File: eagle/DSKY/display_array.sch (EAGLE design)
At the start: 65 parts, among them IC1 PCF8574T, IC10 PCF8574AT, IC2 PCF8574T, IC3 PCF8574T, IC4 PCF8574T, IC5 PCF8574T, IC6 PCF8574T, IC7 PCF8574T, IC8 PCF8574T, IC9 PCF8574AT

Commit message: brightness control
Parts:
- removed RN17: (no value), be_rcl:R_EU_ARRAY_1C_8_T_SIL9
- added C1201, C1202, C1203, C1204, C1301, C1302, C1303, C1304: 10u, be_rcl:C_POL_EU_T_RAD5_GRID_2.54
- added C1205, C1206, C1305, C1306: 100n, be_rcl:C_EU_S_0805
- added H1101, H1102, H1103, H1104: HOLE_4.1_PAD, be_holes:HOLE_4.1_PAD
- added IC1201, IC1202, IC1301, IC1302: (no value), be_logic:7400N
- added RN1001, RN1002: 100, be_rcl:R_EU_ARRAY_4
- added RN1201, RN1202, RN1301, RN1302: 220, be_rcl:R_EU_ARRAY_4
- added RN1203, RN1303: 4k7, be_rcl:R_EU_ARRAY_4
- renumbered C1 to C101, C10 to C1001, C2 to C201, C3 to C301, C4 to C401, C5 to C501, C6 to C601, C7 to C701, C8 to C801, C9 to C901, DIS1 to DIS101, DIS2 to DIS201, DIS3 to DIS301, DIS4 to DIS401, DIS5 to DIS501, DIS6 to DIS601, DIS7 to DIS701, DIS8 to DIS801, IC1 to IC101, IC10 to IC1001, IC2 to IC201, IC3 to IC301, IC4 to IC401, IC5 to IC501, IC6 to IC601, IC7 to IC701, IC8 to IC801, IC9 to IC901, LED1 to LED902, LED10 to LED903, LED12 to LED910, LED2 to LED909, LED3 to LED908, LED4 to LED911, LED5 to LED901, LED6 to LED906, LED7 to LED907, LED8 to LED905, LED9 to LED904, R1 to R909, R2 to R908, R3 to R907, R4 to R906, R5 to R905, R6 to R904, R7 to R903, R8 to R902, R9 to R901, RN1 to RN101, RN10 to RN502, RN11 to RN601, RN12 to RN602, RN13 to RN701, RN14 to RN702, RN15 to RN801, RN16 to RN802, RN2 to RN102, RN3 to RN201, RN4 to RN202, RN5 to RN301, RN6 to RN302, RN7 to RN401, RN8 to RN402, RN9 to RN501
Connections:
- new net DEBOUNCER_10: C1201.+, RN1201A.2, RN1201B.1
- new net DEBOUNCER_11: IC1201A.I0, IC1201A.I1, RN1201B.2, RN1203B.1
- new net DEBOUNCER_12: IC1201A.O, IC1201B.I0, IC1201B.I1
- new net DEBOUNCER_1_OUT#: IC1201B.O, RN1001A.2, RN1203B.2
- new net DEBOUNCER_20: C1202.+, RN1201C.2, RN1201D.1
- new net DEBOUNCER_21: IC1201D.I0, IC1201D.I1, RN1201D.2, RN1203A.1
- new net DEBOUNCER_22: IC1201C.I0, IC1201C.I1, IC1201D.O
- new net DEBOUNCER_2_OUT#: IC1201C.O, RN1001B.2, RN1203A.2
- new net DEBOUNCER_30: C1203.+, RN1202A.2, RN1202B.1
- new net DEBOUNCER_31: IC1202A.I0, IC1202A.I1, RN1202B.2, RN1203C.1
- new net DEBOUNCER_32: IC1202A.O, IC1202B.I0, IC1202B.I1
- new net DEBOUNCER_3_OUT#: IC1202B.O, RN1001C.2, RN1203C.2
- new net DEBOUNCER_40: C1204.+, RN1202C.2, RN1202D.1
- new net DEBOUNCER_41: IC1202D.I0, IC1202D.I1, RN1202D.2, RN1203D.1
- new net DEBOUNCER_42: IC1202C.I0, IC1202C.I1, IC1202D.O
- new net DEBOUNCER_4_OUT#: IC1202C.O, RN1001D.2, RN1203D.2
- new net DEBOUNCER_50: C1301.+, RN1301A.2, RN1301B.1
- new net DEBOUNCER_51: IC1301A.I0, IC1301A.I1, RN1301B.2, RN1303B.1
- new net DEBOUNCER_52: IC1301A.O, IC1301B.I0, IC1301B.I1
- new net DEBOUNCER_5_OUT#: IC1301B.O, RN1002A.2, RN1303B.2
- new net DEBOUNCER_60: C1302.+, RN1301C.2, RN1301D.1
- new net DEBOUNCER_61: IC1301D.I0, IC1301D.I1, RN1301D.2, RN1303A.1
- new net DEBOUNCER_62: IC1301C.I0, IC1301C.I1, IC1301D.O
- new net DEBOUNCER_6_OUT#: IC1301C.O, RN1002B.2, RN1303A.2
- new net DEBOUNCER_70: C1303.+, RN1302A.2, RN1302B.1
- new net DEBOUNCER_71: IC1302A.I0, IC1302A.I1, RN1302B.2, RN1303C.1
- new net DEBOUNCER_72: IC1302A.O, IC1302B.I0, IC1302B.I1
- new net DEBOUNCER_7_OUT#: IC1302B.O, RN1002C.2, RN1303C.2
- new net DEBOUNCER_80: C1304.+, RN1302C.2, RN1302D.1
- new net DEBOUNCER_81: IC1302D.I0, IC1302D.I1, RN1302D.2, RN1303D.1
- new net DEBOUNCER_82: IC1302C.I0, IC1302C.I1, IC1302D.O
- new net DEBOUNCER_8_OUT#: IC1302C.O, RN1002D.2, RN1303D.2
- new net IN_1#: RN1201A.1
- new net IN_2#: RN1201C.1
- new net IN_3#: RN1202A.1
- new net IN_4#: RN1202C.1
- new net IN_5#: RN1301A.1
- new net IN_6#: RN1301C.1
- new net IN_7#: RN1302A.1
- new net IN_8#: RN1302C.1
- net DRV_ANODE: now also LED903.A, LED904.A, LED905.A, LED906.A, LED907.A, LED908.A, LED909.A, LED910.A, LED911.A
- net GND: now also C1201.-, C1202.-, C1203.-, C1204.-, C1205.2, C1206.2, C1301.-, C1302.-, C1303.-, C1304.-, C1305.2, C1306.2, IC1201P.GND, IC1202P.GND, IC1301P.GND, IC1302P.GND
- net KEYPAD_1_K_1: now also RN1001A.1; no longer RN17.2
- net KEYPAD_1_K_2: now also RN1001B.1; no longer RN17.3
- net KEYPAD_1_K_3: now also RN1001C.1; no longer RN17.4
- net KEYPAD_1_K_4: now also RN1001D.1; no longer RN17.5
- net KEYPAD_1_K_5: now also RN1002A.1; no longer RN17.6
- net KEYPAD_1_K_6: now also RN1002B.1; no longer RN17.7
- net KEYPAD_1_K_7: now also RN1002C.1; no longer RN17.8
- net KEYPAD_1_K_8: now also RN1002D.1; no longer RN17.9
- net P5V: now also C1205.1, C1206.1, C1305.1, C1306.1, IC1201P.VCC, IC1202P.VCC, IC1301P.VCC, IC1302P.VCC; no longer LED903.A, LED904.A, LED905.A, LED906.A, LED907.A, LED908.A, LED909.A, LED910.A, LED911.A, RN17.1

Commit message: added connectors
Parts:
- added C1, C2: 100u, be_rcl:C_POL_EU_T_RAD7_GRID_2.54
- added LED1: green, be_opt:LED_S_0805
- added R1: 220, be_rcl:R_EU_S_0805
- added RN1, RN2: (no value), be_rcl:R_EU_ARRAY_1C_8_T_SIL9
- added S1, S2, S3, S4, S5, S6, S7, S8: (no value), be_switch:PUSH_BUTTON_T_6X6MM
- added X1, X3: MALE_2X13-T-VERTICAL_2.54MM, be_con_jump:MALE_2X13-T-VERTICAL_2.54MM
- added X2: CLAMP_1X4-T-5MM, be_con_jump:CLAMP_1X4-T-5MM
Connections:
- new net CTRL_ACK#: RN2.3, X1.19
- new net CTRL_B2: RN1.4, X1.7
- new net CTRL_B3: RN1.5, X1.9
- new net CTRL_B4: RN1.6, X1.11
- new net CTRL_B5: RN1.7, X1.13
- new net CTRL_B6: RN1.8, X1.15
- new net CTRL_B7: RN1.9, X1.17
- new net CTRL_BUSY: RN2.4, X1.21
- new net CTRL_STROBE#: RN2.2, X1.1
- new net P5V_LED: LED1.C, R1.2
- net CTRL_SCL: now also RN1.2, X1.3
- net CTRL_SDA: now also RN1.3, X1.5
- net GND: now also C1.-, C2.-, R1.1, S1.A1, S2.A1, S3.A1, S4.A1, S5.A1, S6.A1, S7.A1, S8.A1, X1.10, X1.12, X1.14, X1.16, X1.18, X1.2, X1.20, X1.22, X1.24, X1.26, X1.4, X1.6, X1.8, X2.3, X2.4, X3.10, X3.12, X3.14, X3.16, X3.18, X3.2, X3.20, X3.22, X3.24, X3.26, X3.4, X3.6, X3.8
- net IN_1#: now also S1.B1, X3.3
- net IN_2#: now also S2.B1, X3.5
- net IN_3#: now also S3.B1, X3.7
- net IN_4#: now also S4.B1, X3.9
- net IN_5#: now also S5.B1, X3.11
- net IN_6#: now also S6.B1, X3.13
- net IN_7#: now also S7.B1, X3.15
- net IN_8#: now also S8.B1, X3.17
- net P5V: now also C1.+, C2.+, LED1.A, RN1.1, RN2.1, X2.1, X2.2

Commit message: reverse voltage protection
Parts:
- added C102: 47n, be_rcl:C_EU_S_0805
- added C103: 10n, be_rcl:C_EU_S_0805
- added C3: 100n, be_rcl:C_EU_S_0805
- added D1: (no value), be_diode:SINGLE_T_DO204-2_GRID_14MM
- added D101: BAT48, be_diode:SINGLE_T_DO204_GRID_10MM
- added IC1: NE555V, be_timer:555P
- added R101: 10k, be_rcl:R_EU_S_0805
- added R102: 470k, be_rcl:R_EU_S_0805
- added R103: 1k, be_rcl:R_EU_S_0805
- added T101, T102: NX2301P, be_transistor:P-MOSFET
- added TP101, TP102: (no value), be_con_jump:TEST_POINT_T_LARGE
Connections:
- removed net DRV_ANODE: DIS101.COM1, DIS201.COM1, DIS301.COM1, DIS401.COM1, DIS501.COM1, DIS601.COM1, DIS701.COM1, DIS801.COM1, LED903.A, LED904.A, LED905.A, LED906.A, LED907.A, LED908.A, LED909.A, LED910.A, LED911.A
- new net DRV_ANODE_1: DIS101.COM1, DIS201.COM1, DIS301.COM1, DIS401.COM1, LED903.A, LED904.A, LED905.A, LED906.A, LED907.A, LED908.A, LED909.A, LED910.A, LED911.A, T101.D
- new net DRV_ANODE_2: DIS501.COM1, DIS601.COM1, DIS701.COM1, DIS801.COM1, T102.D
- new net TIM_1: C103.1, IC1.OC, IC1.RST#
- new net TIM_2: C102.1, D101.C, IC1.TRG, IC1.TRSHLD, R101.1
- new net TIM_3: D101.A, IC1.DSCHRG, R101.2, R102.1, TP102.MP
- new net TIM_OUT: IC1.OUT, R103.1, T101.G, T102.G
- net GND: now also C102.2, C103.2, C3.2, D1.A, IC1.GND
- net P5V: now also C3.1, D1.C, IC1.VCC, R102.2, R103.2, T101.S, T102.S, TP101.MP
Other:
- note added: "LDC terminals"

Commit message: prepared routing of P5V and GND
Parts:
- removed D1: (no value), be_diode:SINGLE_T_DO204-2_GRID_14MM
- removed LED1: green, be_opt:LED_S_0805
- removed R1: 220, be_rcl:R_EU_S_0805
- added D1401: 1N5400, be_diode:SINGLE_T_DO201_GRID_18MM
- added FD1101, FD1102: FIDUCIAL_CROSSHAIR, be_marks:FIDUCIAL_CROSSHAIR
- added LED1401: green, be_opt:LED_S_0805
- added R1401: 220, be_rcl:R_EU_S_0805
- IC1201, IC1202, IC1301, IC1302: value (none) -> SN7400N; PART_CODE_BEL (none) -> IC_PAC_T_NDIP14_VAL_SN7400N
- R901, R902: value (none) -> 1k5; PART_CODE_BEL (none) -> R_PAC_S_0805_VAL_1k5
- R903, R904: value (none) -> 750; PART_CODE_BEL (none) -> R_PAC_S_0805_VAL_750
- R905, R906: value (none) -> 2k2; PART_CODE_BEL (none) -> R_PAC_S_0805_VAL_2k2
- R907: value (none) -> 3k3; PART_CODE_BEL (none) -> R_PAC_S_0805_VAL_3k3
- R908, R909: value (none) -> 2k5; PART_CODE_BEL (none) -> R_PAC_S_0805_VAL_2k5
- RN1401, RN1402: value (none) -> 10k; BOM (none) -> NO
- S1501: value (none) -> set; FUNCTION (none) -> SET1
- S1502: value (none) -> set; FUNCTION (none) -> SET2
- S1503: value (none) -> set; FUNCTION (none) -> SET3
- S1504: value (none) -> set; FUNCTION (none) -> SET4
- S1505: value (none) -> set; FUNCTION (none) -> SET5
- S1506: value (none) -> set; FUNCTION (none) -> SET6
- S1507: value (none) -> set; FUNCTION (none) -> SET7
- S1508: value (none) -> set; FUNCTION (none) -> SET8
- TP1601, TP1602: value (none) -> TEST_POINT_T_LARGE
- X1501: FUNCTION KEYPAD -> KEYPAD EXT,
- renumbered C1 to C1401, C102 to C1602, C103 to C1603, C2 to C1402, C3 to C1601, D101 to D1601, IC1 to IC1601, R101 to R1601, R102 to R1602, R103 to R1603, RN1 to RN1401, RN2 to RN1402, S1 to S1501, S2 to S1502, S3 to S1503, S4 to S1504, S5 to S1505, S6 to S1506, S7 to S1507, S8 to S1508, T101 to T1601, T102 to T1602, TP101 to TP1601, TP102 to TP1602, X1 to X1402, X2 to X1401, X3 to X1501
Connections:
- net DRV_ANODE_2: now also LED1401.A
- net GND: now also D1401.A, H1101.MOUNT, H1102.MOUNT, H1103.MOUNT, H1104.MOUNT, R1401.1; no longer D1.A, R1.1
- net P5V: now also D1401.C; no longer D1.C, LED1.A
- net P5V_LED: now also LED1401.C, R1401.2; no longer LED1.C, R1.2

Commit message: silk screen for keys fixed
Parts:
- added LED1, LED2: red, be_opt:LED_S_0805
- added R1: 1k5, be_rcl:R_EU_S_0805
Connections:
- net N$1 renamed DRV_9_LED_R1BB
- net N$2 renamed DRV_9_LED_R1AA
- new net DRV_9_LED_R1C: LED1.C, R1.2
- new net DRV_9_LED_R1CC: LED1.A, LED2.C
- net DRV_9_LED_1: now also R1.1
- net DRV_ANODE_1: now also LED2.A
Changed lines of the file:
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@@
 <part name="GND61" library="be_supply" deviceset="GND" device=""/>
 <part name="GND62" library="be_supply" deviceset="GND" device=""/>
+<part name="R1" library="be_rcl" deviceset="R_EU" device="_S_0805" value="1k5">
+<attribute name="PART_CODE_BEL" value="R_PAC_S_0805_VAL_1k5"/>
+</part>
+<part name="LED1" library="be_opt" deviceset="LED" device="_S_0805" value="red">
+<attribute name="PART_CODE_BEL" value="LED_PAC_S_0805_VAL_red"/>
+</part>
+<part name="LED2" library="be_opt" deviceset="LED" device="_S_0805" value="red">
+<attribute name="PART_CODE_BEL" value="LED_PAC_S_0805_VAL_red"/>
+</part>
 </parts>
 <sheets>
@@
 <attribute name="VALUE" x="170.815" y="102.235" size="1.27" layer="96" font="fixed"/>
 </instance>
+<instance part="R1" gate="G$1" x="134.62" y="142.24"/>
+<instance part="LED1" gate="G$1" x="170.18" y="142.24" smashed="yes" rot="R270">
+<attribute name="NAME" x="170.815" y="143.51" size="1.27" layer="95" font="fixed"/>
+<attribute name="VALUE" x="170.815" y="140.335" size="1.27" layer="96" font="fixed"/>
+</instance>
+<instance part="LED2" gate="G$1" x="182.88" y="142.24" smashed="yes" rot="R270">
+<attribute name="NAME" x="183.515" y="143.51" size="1.27" layer="95" font="fixed"/>
+<attribute name="VALUE" x="183.515" y="140.335" size="1.27" layer="96" font="fixed"/>
+</instance>
 </instances>
 <busses>
@@
 <wire x1="127" y1="134.62" x2="127" y2="127" width="0.1524" layer="91"/>
 <junction x="127" y="127"/>
+<pinref part="R1" gate="G$1" pin="1"/>
+<wire x1="129.54" y1="142.24" x2="127" y2="142.24" width="0.1524" layer="91"/>
+<wire x1="127" y1="142.24" x2="127" y2="134.62" width="0.1524" layer="91"/>
+<junction x="127" y="134.62"/>
 </segment>
 </net>
@@
 </segment>
 </net>
-<net name="N$1" class="0">
+<net name="DRV_9_LED_R1BB" class="0">
 <segment>
 <pinref part="LED911" gate="G$1" pin="C"/>
@@
 </segment>
 </net>
-<net name="N$2" class="0">
+<net name="DRV_9_LED_R1AA" class="0">
 <segment>
 <pinref part="LED910" gate="G$1" pin="C"/>
@@
 <pinref part="LED909" gate="G$1" pin="A"/>
 <label x="208.28" y="127" size="1.27" layer="95" font="fixed" xref="yes"/>
-</segment>
-</net>
+<pinref part="LED2" gate="G$1" pin="A"/>
+<wire x1="185.42" y1="142.24" x2="193.04" y2="142.24" width="0.1524" layer="91"/>
+<wire x1="193.04" y1="142.24" x2="193.04" y2="134.62" width="0.1524" layer="91"/>
+<junction x="193.04" y="134.62"/>
+</segment>
+</net>
+<net name="DRV_9_LED_R1C" class="0">
+<segment>
+<pinref part="R1" gate="G$1" pin="2"/>
+<pinref part="LED1" gate="G$1" pin="C"/>
+<wire x1="139.7" y1="142.24" x2="165.1" y2="142.24" width="0.1524" layer="91"/>
+<label x="142.875" y="142.875" size="1.27" layer="95" font="fixed"/>
+</segment>
+</net>
+<net name="DRV_9_LED_R1CC" class="0">
+<segment>
+<pinref part="LED1" gate="G$1" pin="A"/>
+<pinref part="LED2" gate="G$1" pin="C"/>
+<wire x1="172.72" y1="142.24" x2="177.8" y2="142.24" width="0.1524" layer="91"/>
+</segment>
+</net>

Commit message: fixed attributes
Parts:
- removed LED1, LED2: red, be_opt:LED_S_0805
- removed R1: 1k5, be_rcl:R_EU_S_0805
- added C1604: 10n, be_rcl:C_EU_S_0805
- added LED912, LED913: red, be_opt:LED_S_0805
- added R910: 2k5, be_rcl:R_EU_S_0805
- C1602: value 47n -> 100n; PART_CODE_BEL C_PAC_S_0805_VAL_47n -> C_PAC_S_0805_VAL_100n
- C1603: value 10n -> 100n; PART_CODE_BEL C_PAC_S_0805_VAL_10n -> C_PAC_S_0805_VAL_100n
- D1601: PART_CODE_BEL (none) -> D_PAC_T_DO204_GRID_10mm_VAL_BAT48
- DIS101: FUNCTION (none) -> digit 10^0
- DIS201: FUNCTION (none) -> digit 10^1
- DIS301: FUNCTION (none) -> digit 10^2
- DIS401: FUNCTION (none) -> digit 10^3
- DIS501: FUNCTION (none) -> digit 10^4
- DIS601: FUNCTION (none) -> digit 10^5
- DIS701: FUNCTION (none) -> digit 10^6
- DIS801: FUNCTION (none) -> digit 10^7
- IC1001, IC901: PART_CODE_BEL IC_PAC_S_SIOC16_VAL_PCF8574AT -> IC_PAC_S_SOIC16_VAL_PCF8574AT
- LED901, LED902, LED911: FUNCTION (none) -> blinking dot
- LED903: value green -> red; FUNCTION (none) -> blinking dot; PART_CODE_BEL LED_PAC_S_0805_VAL_green -> LED_PAC_S_0805_VAL_red
- LED904: FUNCTION (none) -> status #1
- LED905: value yellow -> green; FUNCTION (none) -> status #2; PART_CODE_BEL LED_PAC_S_0805_VAL_yellow -> LED_PAC_S_0805_VAL_green
- LED906: FUNCTION (none) -> status #3
- LED907: value red -> yellow; FUNCTION (none) -> status #4; PART_CODE_BEL LED_PAC_S_0805_VAL_red -> LED_PAC_S_0805_VAL_yellow
- LED908: value blue -> red; FUNCTION (none) -> status #5; PART_CODE_BEL LED_PAC_S_0805_VAL_blue -> LED_PAC_S_0805_VAL_red
- LED909: FUNCTION (none) -> status #6
- LED910: value red -> blue; FUNCTION (none) -> status #7; PART_CODE_BEL LED_PAC_S_0805_VAL_red -> LED_PAC_S_0805_VAL_blue
- R903: value 750 -> 1k5; PART_CODE_BEL R_PAC_S_0805_VAL_750 -> R_PAC_S_0805_VAL_1k5
- R905: value 2k2 -> 750; PART_CODE_BEL R_PAC_S_0805_VAL_2k2 -> R_PAC_S_0805_VAL_750
- R907: value 3k3 -> 2k2; PART_CODE_BEL R_PAC_S_0805_VAL_3k3 -> R_PAC_S_0805_VAL_2k2
- R908: value 2k5 -> 3k3; PART_CODE_BEL R_PAC_S_0805_VAL_2k5 -> R_PAC_S_0805_VAL_3k3
- RN1201, RN1202, RN1301, RN1302: PART_CODE_BEL (none) -> RN_PAC_T_SIL8_VAL_220
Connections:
- new net N$1: C1602.2, C1603.1
- net DRV_9_LED_1: now also R903.1; no longer R1.1
- net DRV_9_LED_2: now also R904.1; no longer R903.1
- net DRV_9_LED_3: now also R905.1; no longer R904.1
- net DRV_9_LED_4: now also R906.1; no longer R905.1
- net DRV_9_LED_5: now also R907.1; no longer R906.1
- net DRV_9_LED_6: now also R908.1; no longer R907.1
- net DRV_9_LED_7: now also R909.1; no longer R908.1
- net DRV_9_LED_8: now also R910.1; no longer R909.1
- net DRV_9_LED_R1A: now also LED902.C, R902.2; no longer LED901.C, R901.2
- net DRV_9_LED_R1AA: now also LED902.A, LED912.C; no longer LED901.A, LED910.C
- net DRV_9_LED_R1B: now also LED903.C, R903.2; no longer LED902.C, R902.2
- net DRV_9_LED_R1BB: now also LED903.A, LED913.C; no longer LED902.A, LED911.C
- net DRV_9_LED_R1C: now also LED901.C, R901.2; no longer LED1.C, R1.2
- net DRV_9_LED_R1CC: now also LED901.A, LED911.C; no longer LED1.A, LED2.C
- net DRV_9_LED_R2: now also LED904.C, R904.2; no longer LED903.C, R903.2
- net DRV_9_LED_R3: now also LED905.C, R905.2; no longer LED904.C, R904.2
- net DRV_9_LED_R4: now also LED906.C, R906.2; no longer LED905.C, R905.2
- net DRV_9_LED_R5: now also LED907.C, R907.2; no longer LED906.C, R906.2
- net DRV_9_LED_R6: now also LED908.C, R908.2; no longer LED907.C, R907.2
- net DRV_9_LED_R7: now also LED909.C, R909.2; no longer LED908.C, R908.2
- net DRV_9_LED_R8: now also LED910.C, R910.2; no longer LED909.C, R909.2
- net DRV_ANODE_1: now also LED912.A, LED913.A; no longer LED2.A, LED903.A
- net GND: now also C1604.2; no longer C1602.2
- net TIM_1: now also C1604.1; no longer C1603.1
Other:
- moved on the sheet: C1602, C1603, LED901, LED902, LED903, LED904, LED905, LED906, LED907, LED908, LED909, LED910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

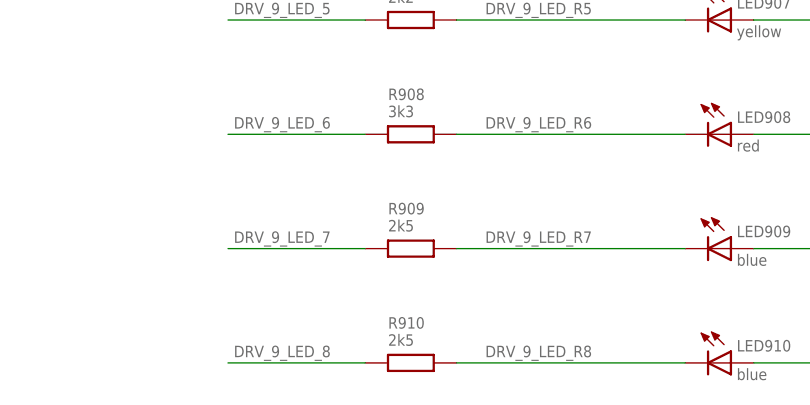
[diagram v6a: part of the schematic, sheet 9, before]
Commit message: -routed supply -applied dru Q-Print standard
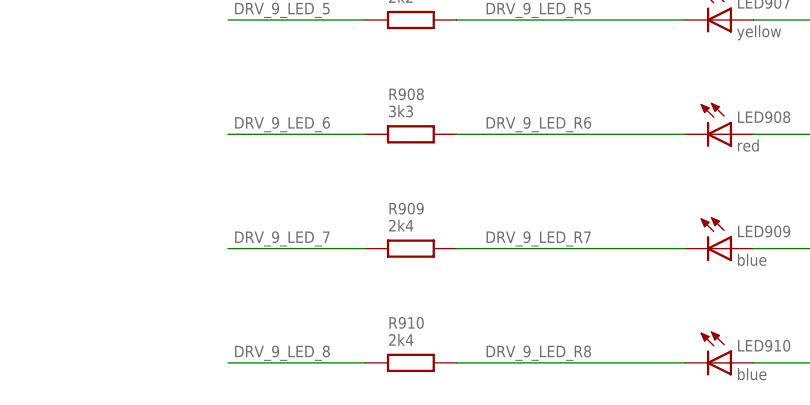
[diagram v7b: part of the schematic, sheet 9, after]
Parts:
- R909, R910: value 2k5 -> 2k4; PART_CODE_BEL R_PAC_S_0805_VAL_2k5 -> R_PAC_S_0805_VAL_2k4
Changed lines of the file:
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@@
 </part>
 <part name="GND27" library="be_supply" deviceset="GND" device=""/>
-<part name="R910" library="be_rcl" deviceset="R_EU" device="_S_0805" value="2k5">
-<attribute name="PART_CODE_BEL" value="R_PAC_S_0805_VAL_2k5"/>
+<part name="R910" library="be_rcl" deviceset="R_EU" device="_S_0805" value="2k4">
+<attribute name="PART_CODE_BEL" value="R_PAC_S_0805_VAL_2k4"/>
 </part>
-<part name="R909" library="be_rcl" deviceset="R_EU" device="_S_0805" value="2k5">
-<attribute name="PART_CODE_BEL" value="R_PAC_S_0805_VAL_2k5"/>
+<part name="R909" library="be_rcl" deviceset="R_EU" device="_S_0805" value="2k4">
+<attribute name="PART_CODE_BEL" value="R_PAC_S_0805_VAL_2k4"/>
 </part>
 <part name="R908" library="be_rcl" deviceset="R_EU" device="_S_0805" value="3k3">

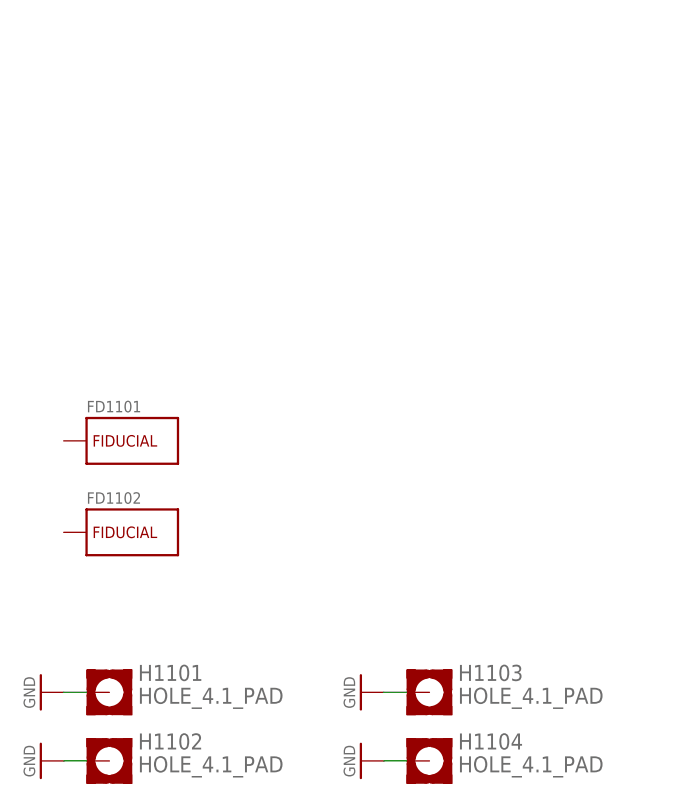
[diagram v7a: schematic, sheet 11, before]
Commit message: fixed silk screen issues
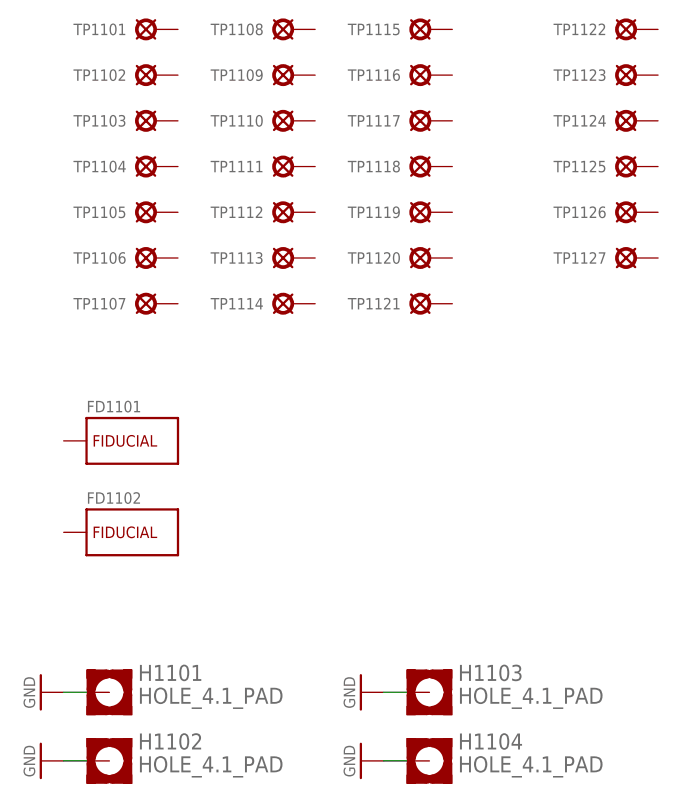
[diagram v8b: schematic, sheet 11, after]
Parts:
- added TP1101, TP1102, TP1103, TP1104, TP1105, TP1106, TP1107, TP1108, TP1109, TP1110, TP1111, TP1112, TP1113, TP1114, TP1115, TP1116, TP1117, TP1118, TP1119, TP1120, TP1121, TP1122, TP1123, TP1124, TP1125, TP1126, TP1127, TP1401, TP1402, TP1603, TP1604, TP1607: TEST_POINT_T_SMALL, be_con_jump:TEST_POINT_T_SMALL
- added TP1605, TP1606: TEST_POINT_T_LARGE, be_con_jump:TEST_POINT_T_LARGE
- added X1403: MALE_1X3, be_con_jump:MALE_1X3
- TP1601, TP1602: value TEST_POINT_T_LARGE -> TEST_POINT_T_SMALL; device be_con_jump:TEST_POINT_T_LARGE -> be_con_jump:TEST_POINT_T_SMALL
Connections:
- net N$1 renamed TIM_45
- net CTRL_SCL: now also TP1401.TP
- net CTRL_SDA: now also TP1402.TP
- net GND: now also TP1603.TP, X1403.1
- net P5V: now also TP1602.TP, TP1605.TP, X1403.3; no longer TP1601.MP
- net TIM_1: now also TP1604.TP
- net TIM_2: now also TP1601.TP
- net TIM_3: now also TP1606.TP; no longer TP1602.MP
- net TIM_OUT: now also TP1607.TP
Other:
- moved on the sheet: TP1601, TP1602
